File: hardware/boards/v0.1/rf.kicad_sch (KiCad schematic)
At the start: 8 parts, among them U22 nRF, U27 ESP32-S3-MINI-1U, Y2 32.768kHz

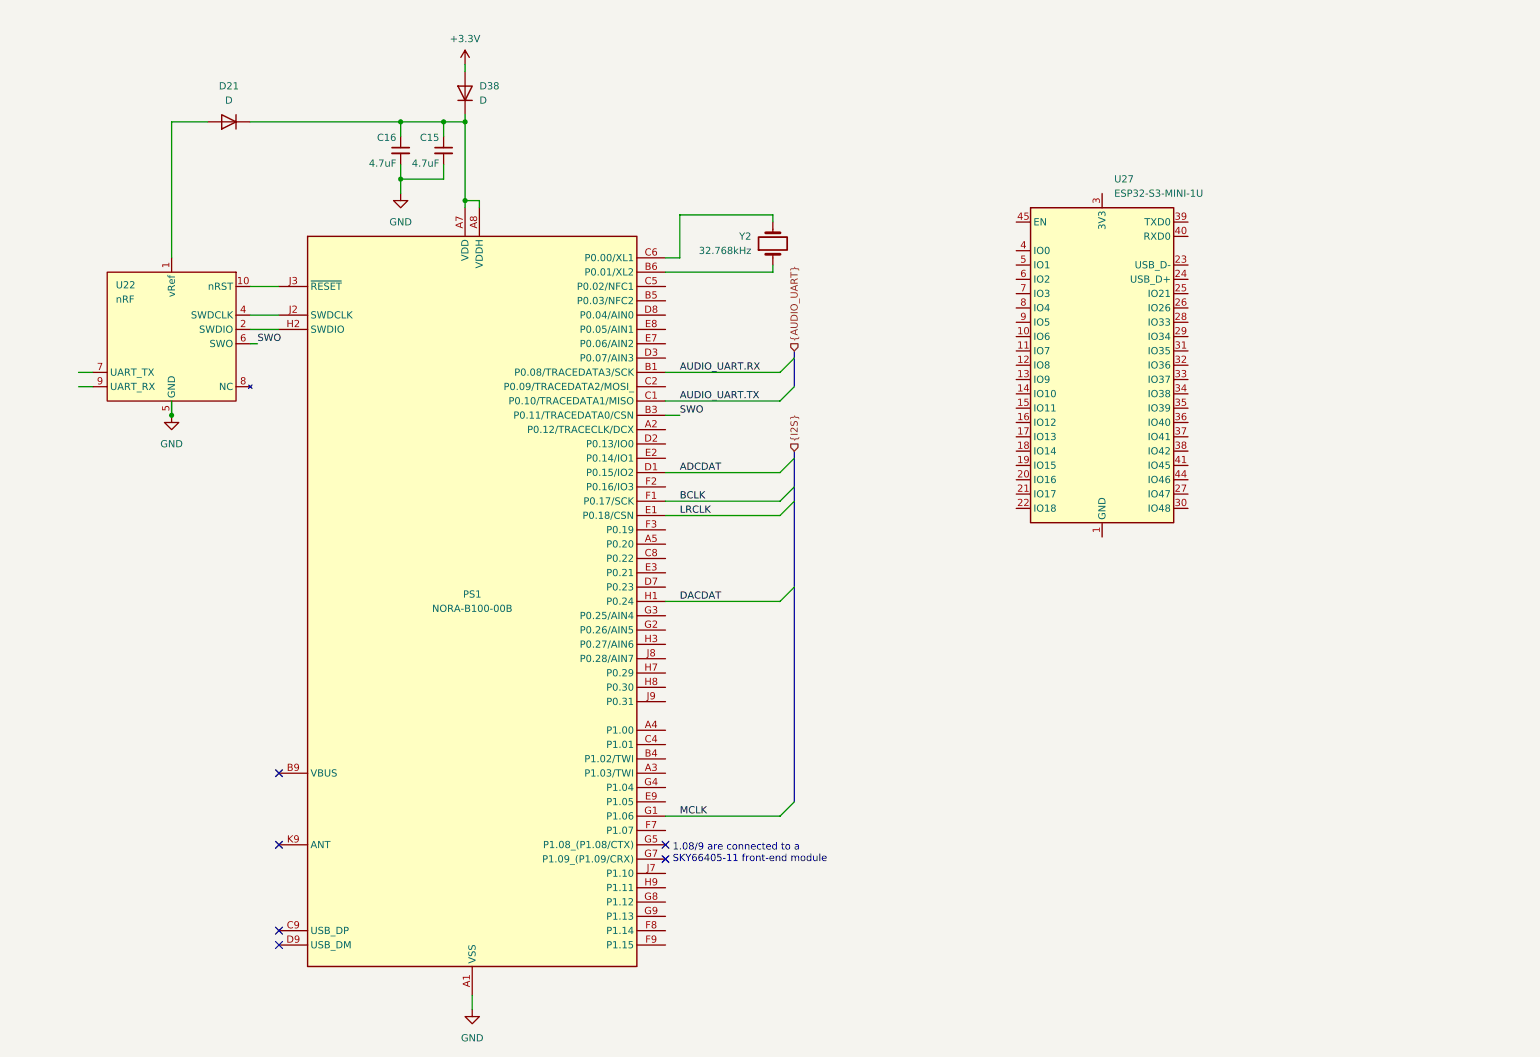
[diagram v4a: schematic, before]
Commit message: feat: various routing and organization
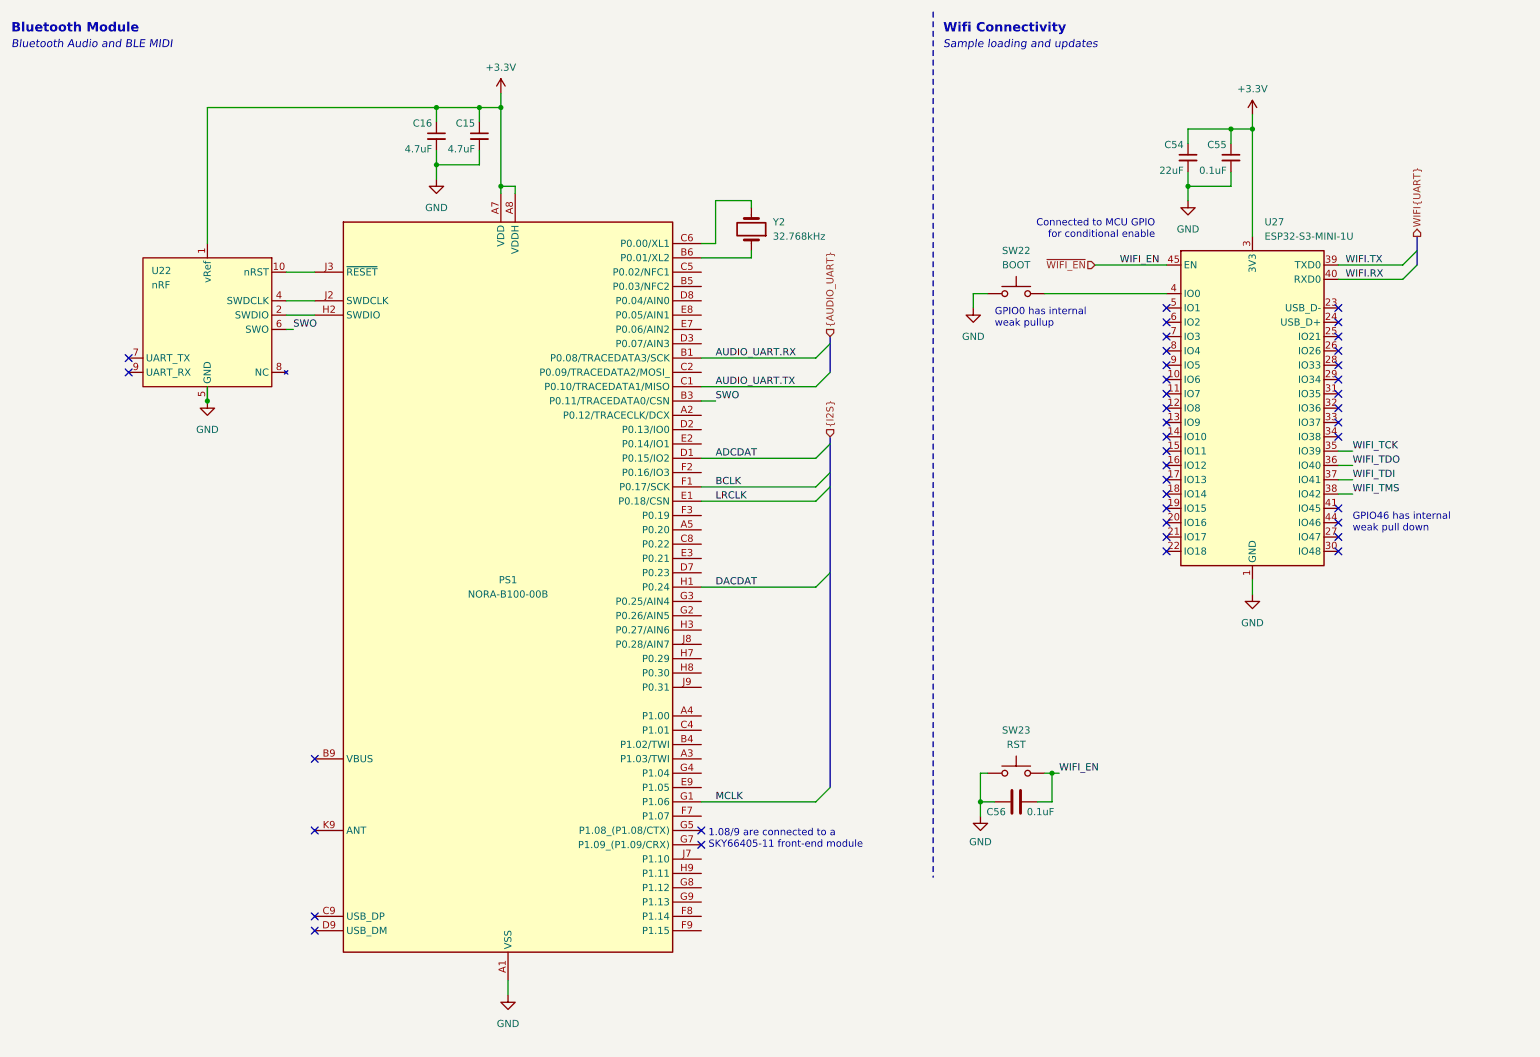
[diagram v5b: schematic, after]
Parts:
- removed D21, D38: D, Diode_SMD:D_0402_1005Metric, symbol Device:D
- added C54: 22uF, Capacitor_SMD:C_0402_1005Metric, symbol Device:C_Small
- added C55: 0.1uF, Capacitor_SMD:C_0402_1005Metric, symbol Device:C_Small
- added C56: 0.1uF, symbol Device:C
- added SW22: BOOT, Button_Switch_SMD:SW_SPST_B3U-1000P, symbol Switch:SW_Push
- added SW23: RST, symbol Switch:SW_Push
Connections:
- net +3.3V: now also C15.1, C16.1, PS1.A7 (VDD), PS1.A8 (VDDH), PS1.B7 (VDD_2), U22.1 (vRef), U27.3 (3V3), C54.1, C55.1
- net GND: now also U27.1 (GND), U27.2 (GND), U27.42 (GND), U27.43 (GND), U27.46 (GND), U27.47 (GND), U27.48 (GND), U27.49 (GND), U27.50 (GND), U27.51 (GND), U27.52 (GND), U27.53 (GND), U27.54 (GND), U27.55 (GND), U27.56 (GND), U27.57 (GND), U27.58 (GND), U27.59 (GND), U27.60 (GND), U27.61 (GND), U27.62 (GND), U27.63 (GND), U27.64 (GND), U27.65 (GND), C54.2, C55.2, C56.1, SW22.1, SW23.1
- net WIFI_TCK: now reaches U27.35 (IO39)
- net WIFI_TDO: now reaches U27.36 (IO40)
- net WIFI_TDI: now reaches U27.37 (IO41)
- net WIFI_TMS: now reaches U27.38 (IO42)
- net WIFI.TX: now reaches U27.39 (TXD0)
- net at U27.4 (IO0): now also SW22.2
- net WIFI.RX: now reaches U27.40 (RXD0)
- net ~{WIFI_EN}: now reaches U27.45 (EN)
- net ~{WIFI_EN}: now also C56.2, SW23.2
- no-connect marks 6 -> 40
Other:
- note added: "Bluetooth Audio and BLE MIDI"
- note added: "Bluetooth Module"
- note added: "Connected to MCU GPIO for conditional enable"
- note added: "GPIO0 has internal weak pullup"
- note added: "GPIO46 has internal weak pull down"
- note added: "Sample loading and updates"
- note added: "Wifi Connectivity"
- moved on the sheet: C15, C16, PS1, U22, U27, Y2

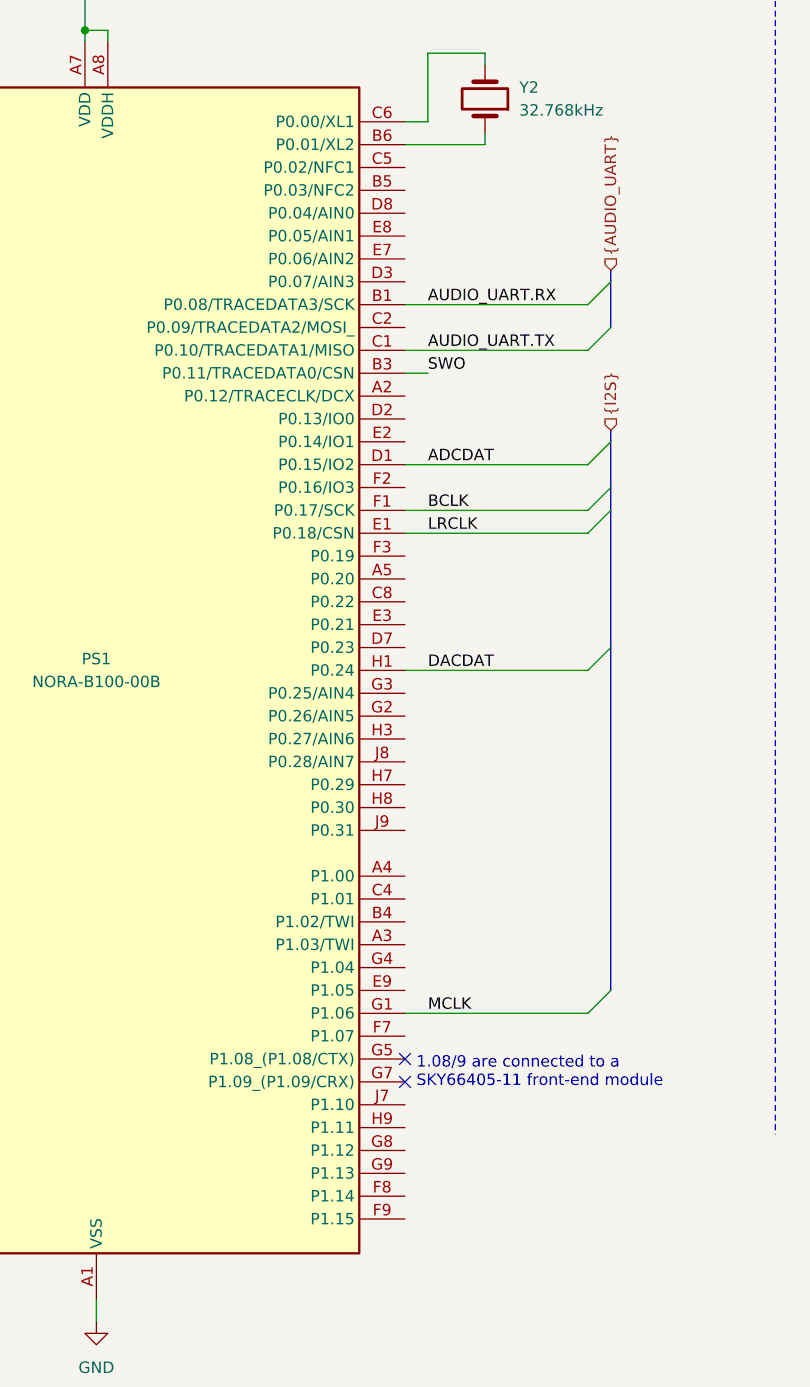
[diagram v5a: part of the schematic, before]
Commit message: feat: schematic organization and ERC cleanup
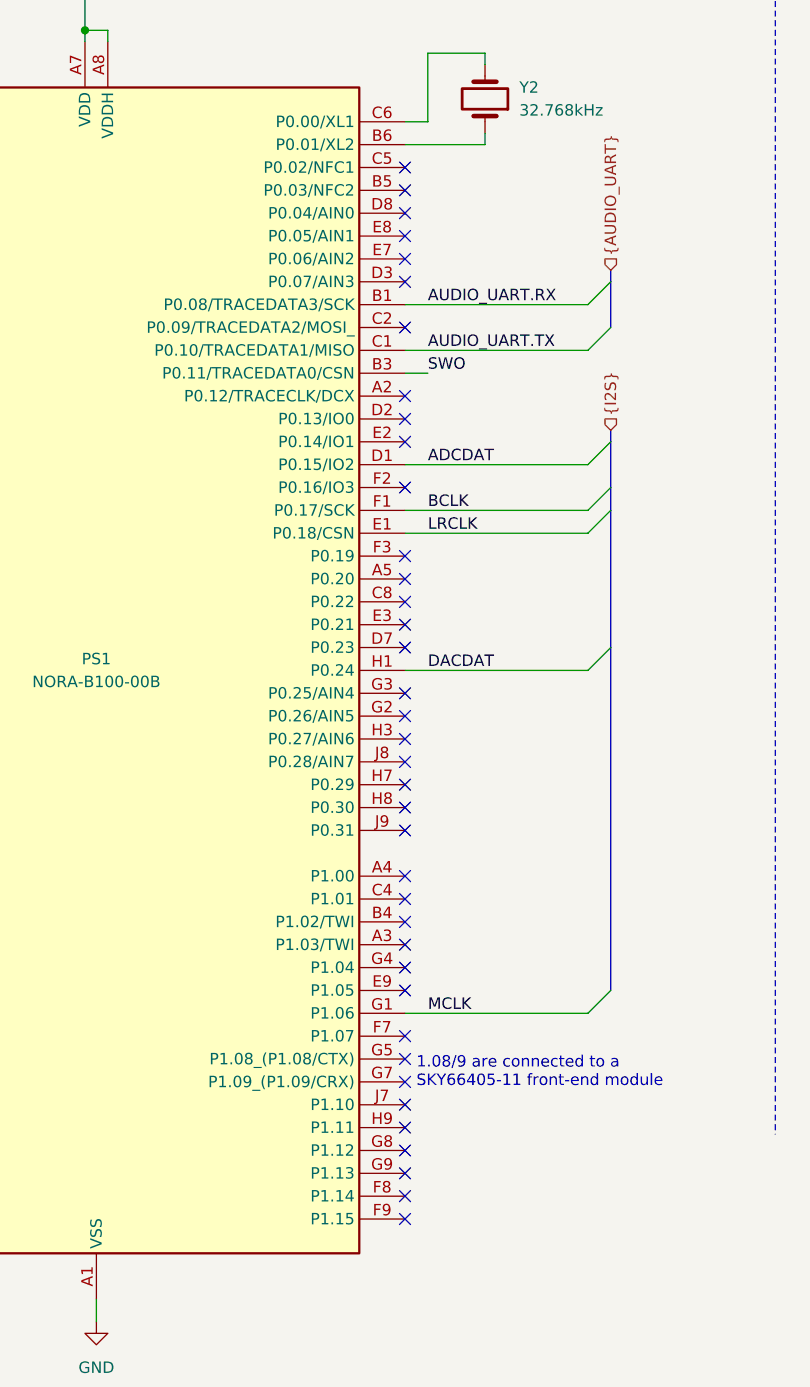
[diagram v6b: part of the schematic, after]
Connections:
- no-connect marks 40 -> 76
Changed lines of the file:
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@@
+	)
+	(no_connect
+		(at 135.89 127)
 	)
 	(no_connect
@@
 	)
 	(no_connect
+		(at 135.89 175.26)
+	)
+	(no_connect
 		(at 248.92 107.95)
 	)
 	(no_connect
+		(at 135.89 101.6)
+	)
+	(no_connect
 		(at 135.89 157.48)
 	)
@@
 	)
 	(no_connect
+		(at 135.89 93.98)
+	)
+	(no_connect
+		(at 135.89 63.5)
+	)
+	(no_connect
 		(at 218.44 100.33)
 	)
@@
 	)
 	(no_connect
+		(at 135.89 144.78)
+	)
+	(no_connect
+		(at 135.89 137.16)
+	)
+	(no_connect
 		(at 218.44 90.17)
 	)
 	(no_connect
+		(at 135.89 142.24)
+	)
+	(no_connect
 		(at 34.29 73.66)
 	)
 	(no_connect
+		(at 135.89 172.72)
+	)
+	(no_connect
 		(at 248.92 100.33)
 	)
@@
 	)
 	(no_connect
+		(at 135.89 124.46)
+	)
+	(no_connect
 		(at 248.92 85.09)
 	)
@@
 	)
 	(no_connect
+		(at 135.89 106.68)
+	)
+	(no_connect
+		(at 135.89 121.92)
+	)
+	(no_connect
 		(at 248.92 105.41)
 	)
 	(no_connect
+		(at 135.89 60.96)
+	)
+	(no_connect
 		(at 248.92 87.63)
 	)
@@
 	)
 	(no_connect
+		(at 135.89 83.82)
+	)
+	(no_connect
 		(at 218.44 102.87)
 	)
 	(no_connect
+		(at 135.89 170.18)
+	)
+	(no_connect
 		(at 248.92 102.87)
 	)
 	(no_connect
+		(at 135.89 129.54)
+	)
+	(no_connect
 		(at 218.44 107.95)
 	)
 	(no_connect
+		(at 135.89 167.64)
+	)
+	(no_connect
+		(at 135.89 139.7)
+	)
+	(no_connect
+		(at 135.89 88.9)
+	)
+	(no_connect
+		(at 135.89 86.36)
+	)
+	(no_connect
+		(at 135.89 119.38)
+	)
+	(no_connect
+		(at 135.89 111.76)
+	)
+	(no_connect
 		(at 248.92 80.01)
 	)
@@
 	)
 	(no_connect
+		(at 135.89 58.42)
+	)
+	(no_connect
+		(at 135.89 66.04)
+	)
+	(no_connect
 		(at 218.44 97.79)
 	)
@@
 	)
 	(no_connect
+		(at 135.89 68.58)
+	)
+	(no_connect
+		(at 135.89 116.84)
+	)
+	(no_connect
 		(at 218.44 64.77)
 	)
 	(no_connect
+		(at 135.89 154.94)
+	)
+	(no_connect
+		(at 135.89 165.1)
+	)
+	(no_connect
 		(at 218.44 85.09)
 	)
@@
 	)
 	(no_connect
+		(at 135.89 104.14)
+	)
+	(no_connect
+		(at 135.89 147.32)
+	)
+	(no_connect
 		(at 67.31 175.26)
 	)
 	(no_connect
+		(at 135.89 132.08)
+	)
+	(no_connect
 		(at 218.44 67.31)
 	)
@@
 	)
 	(no_connect
+		(at 135.89 71.12)
+	)
+	(no_connect
 		(at 218.44 69.85)
 	)
 	(no_connect
+		(at 135.89 109.22)
+	)
+	(no_connect
+		(at 135.89 149.86)
+	)
+	(no_connect
 		(at 34.29 76.2)
 	)
@@
 	)
 	(no_connect
+		(at 135.89 76.2)
+	)
+	(no_connect
 		(at 67.31 144.78)
 	)
@@
 		(at 218.44 105.41)
 	)
+	(no_connect
+		(at 135.89 162.56)
+	)
 	(bus_entry

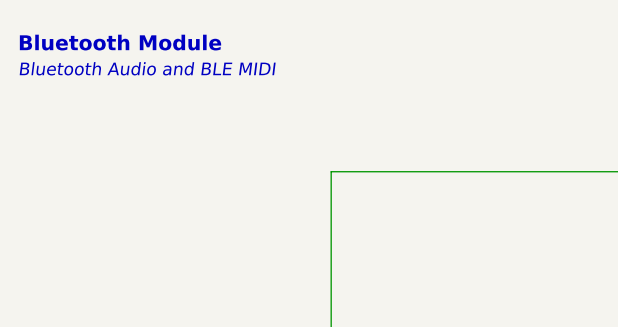
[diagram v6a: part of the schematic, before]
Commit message: chpre: remove extraneous ground vias
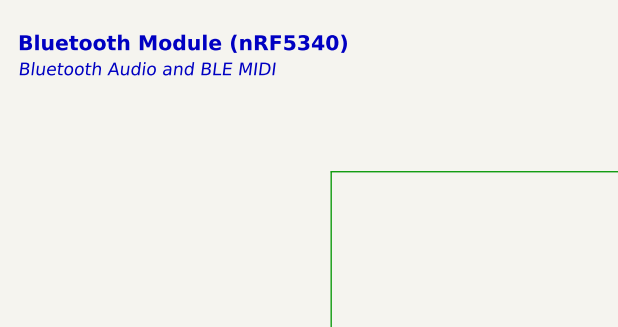
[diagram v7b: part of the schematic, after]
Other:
- note added: "Bluetooth Module (nRF5340)"
- note removed: "Bluetooth Module"
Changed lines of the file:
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@@
 		)
 	)
-	(text "Bluetooth Module"
+	(text "Bluetooth Module (nRF5340)"
 		(exclude_from_sim no)
 		(at 13.462 14.224 0)

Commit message: fix: more ERC cleanup
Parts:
- added J1: WIFI_JTAG, symbol Connector:Conn_ARM_JTAG_SWD_10
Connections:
- net +3.3V: now also J1.1 (VTref)
- net GND: now also J1.3 (GND), J1.5 (GND), J1.9 (GNDDetect)
- net WIFI_TCK: now also J1.4 (SWCLK/TCK)
- net WIFI_TDI: now also J1.8 (NC/TDI)
- net WIFI_TDO: now also J1.6 (SWO/TDO)
- net WIFI_TMS: now also J1.2 (SWDIO/TMS)
- now unconnected: PS1.A6 (N/C_1), PS1.J1 (N/C_2), PS1.J4 (N/C_3), PS1.J5 (N/C_4), PS1.K1 (N/C_5)
